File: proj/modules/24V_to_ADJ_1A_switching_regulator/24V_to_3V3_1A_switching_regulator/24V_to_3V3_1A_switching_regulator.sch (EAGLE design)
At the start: 10 parts, among them U1 MIC4680YM-TR

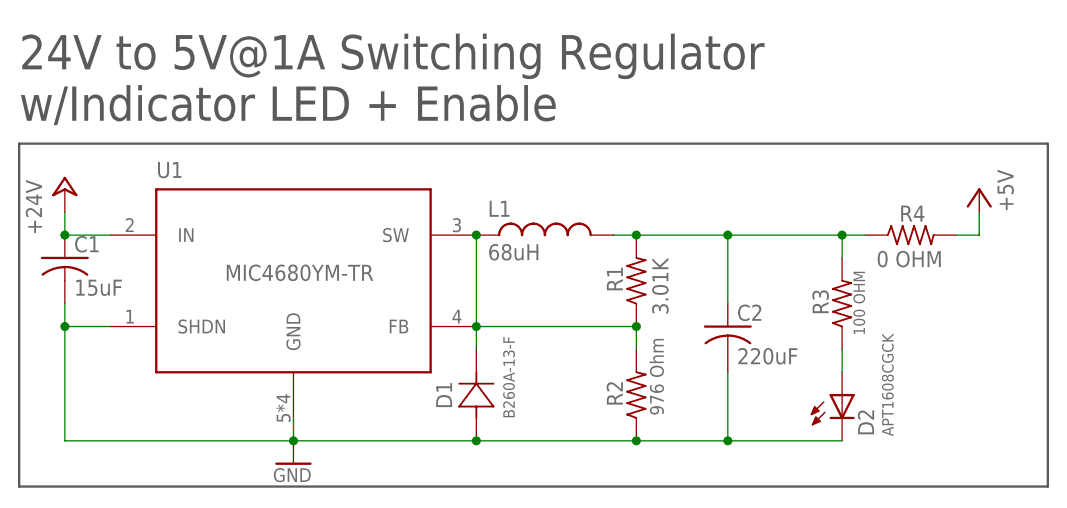
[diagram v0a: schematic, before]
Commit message: cleaned up values and added 1.8V and 3.3V output options
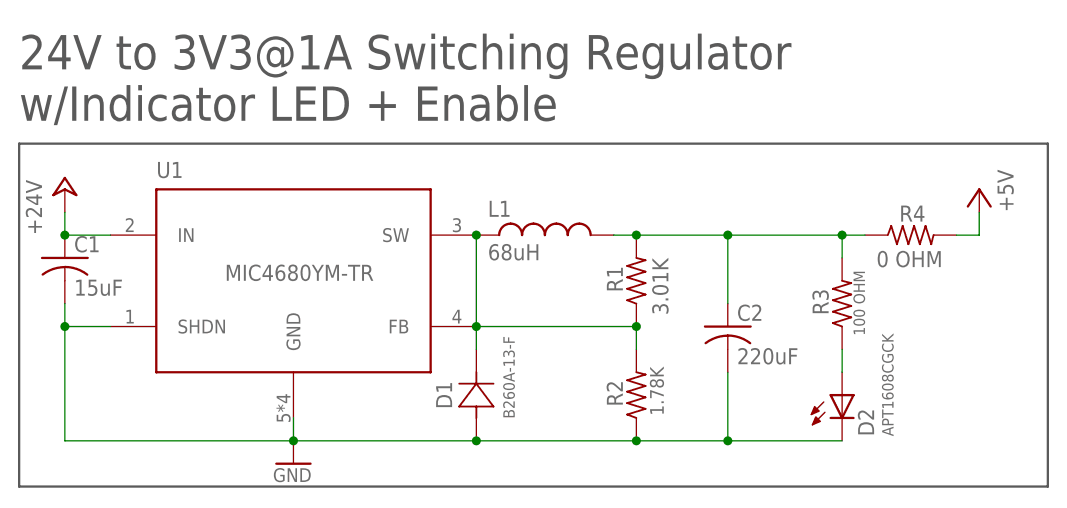
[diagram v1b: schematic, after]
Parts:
- R2: value 976 Ohm -> 1.78K; device openag-resistors:982OHM-RC0603FR-07976RL -> openag-resistors:1.78K-RC0603FR-071K78L
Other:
- note added: "24V to 3V3@1A Switching Regulator w/Indicator LED + Enable"
- note removed: "24V to 5V@1A Switching Regulator w/Indicator LED + Enable"
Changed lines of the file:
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@@
 <part name="D1" library="openag-diodes" deviceset="B260A-13-F" device="" value="B260A-13-F"/>
 <part name="R1" library="openag-resistors" deviceset="3.01K-RC0603FR-073K01L" device="" value="3.01K"/>
-<part name="R2" library="openag-resistors" deviceset="982OHM-RC0603FR-07976RL" device="" value="976 Ohm"/>
+<part name="R2" library="openag-resistors" deviceset="1.78K-RC0603FR-071K78L" device="" value="1.78K"/>
 <part name="GND1" library="openag-supply" deviceset="GND" device=""/>
 <part name="P+1" library="openag-supply" deviceset="+24V" device=""/>
@@
 <sheet>
 <plain>
-<text x="0" y="40.64" size="3.81" layer="97">24V to 5V@1A Switching Regulator
+<text x="0" y="40.64" size="3.81" layer="97">24V to 3V3@1A Switching Regulator
 w/Indicator LED + Enable</text>
 <wire x1="0" y1="38.1" x2="114.3" y2="38.1" width="0.254" layer="97"/>
